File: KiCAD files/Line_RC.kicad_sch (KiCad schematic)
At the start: 26 parts, among them IC1 ESP32-WROVER-E-N4R8, IC2 CP2102N-A02-GQFN28R, IC3 BC847BDW1T1G

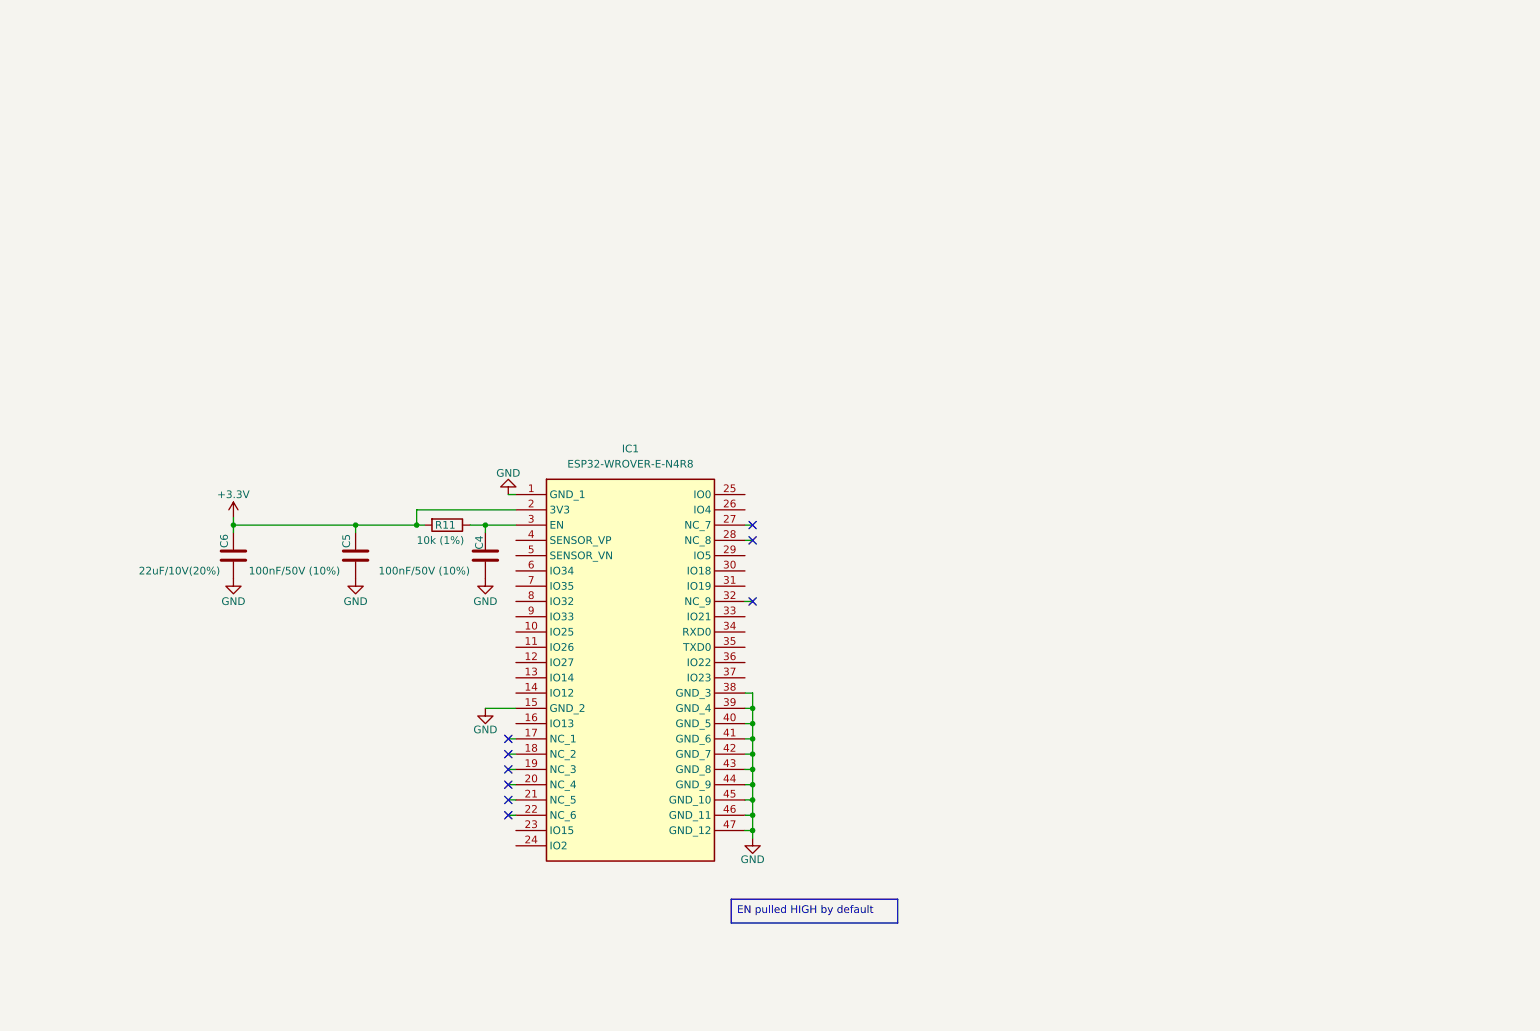
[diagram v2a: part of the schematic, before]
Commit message: Added power connectors
Added the power connectors for the LiPo battery and the ESC. Also added header pins for the selection of the internal / external Buck converter.
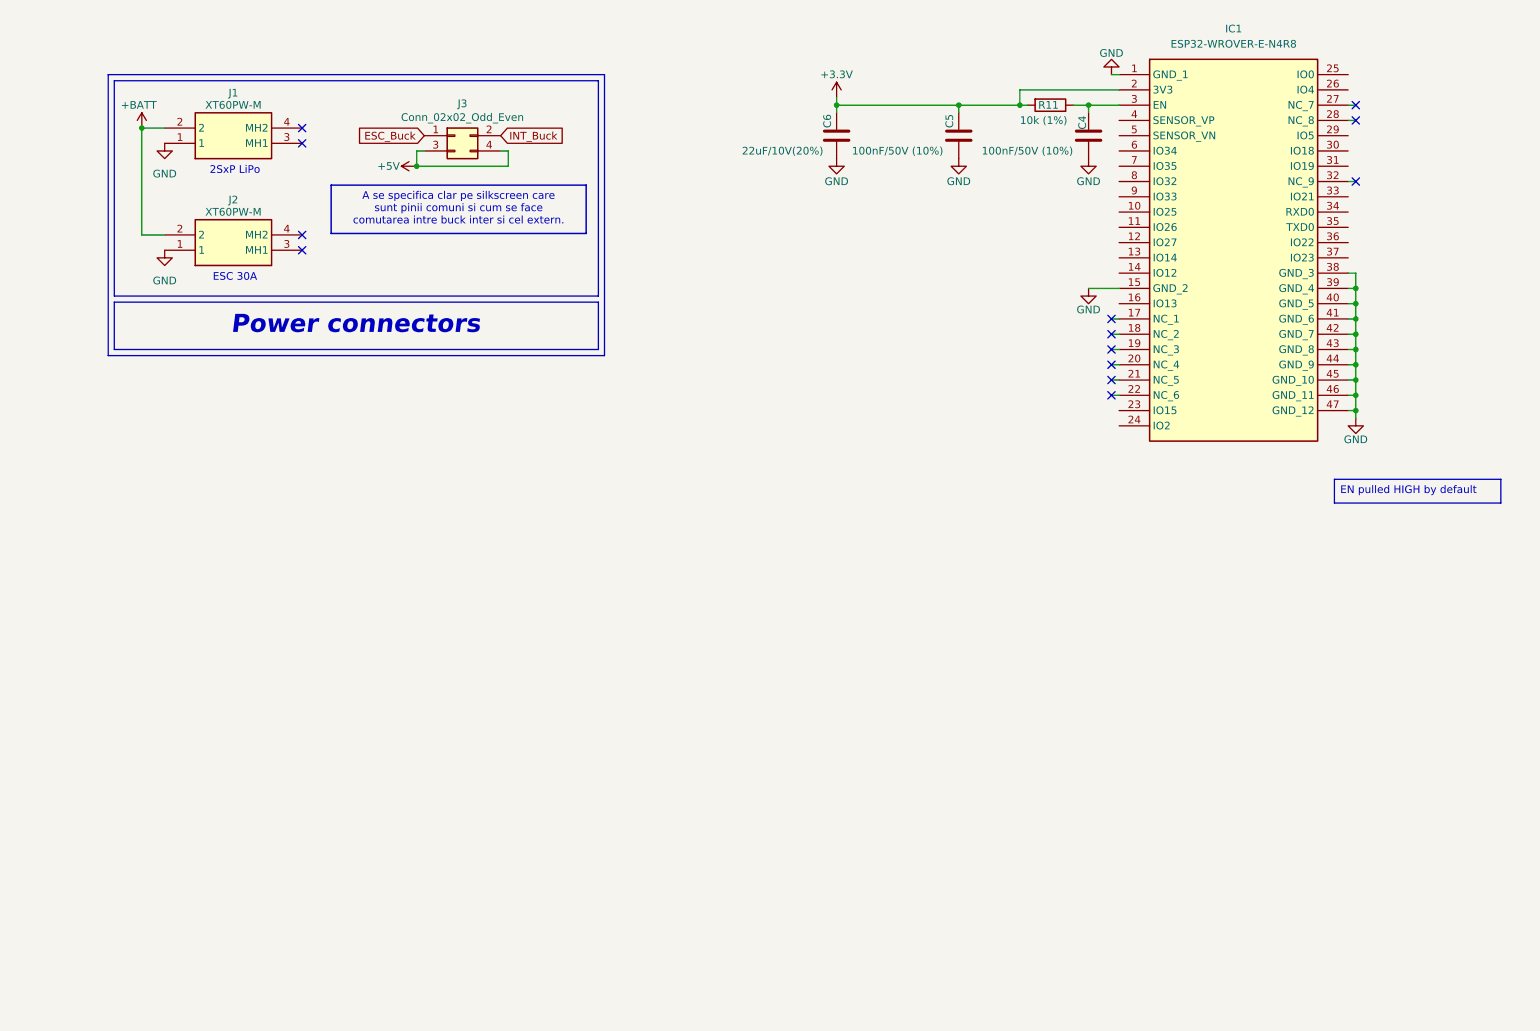
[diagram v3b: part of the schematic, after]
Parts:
- added J1, J2: XT60PW-M, XT60PWM, symbol XT60PW-M:XT60PW-M
- added J3: Conn_02x02_Odd_Even, Connector_PinHeader_1.27mm:PinHeader_2x02_P1.27mm_Vertical, symbol Connector_Generic:Conn_02x02_Odd_Even
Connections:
- net +5V: now also J3.3 (Pin_3), J3.4 (Pin_4)
- net GND: now also J1.1, J2.1
- new net +BATT: J1.2, J2.2
- new net ESC_Buck: J3.1 (Pin_1)
- new net INT_Buck: J3.2 (Pin_2)
- no-connect marks 29 -> 33
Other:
- note added: "2SxP LiPo"
- note added: "ESC 30A"
- note added: "Power connectors"
- moved on the sheet: C4, C5, C6, IC1, R11

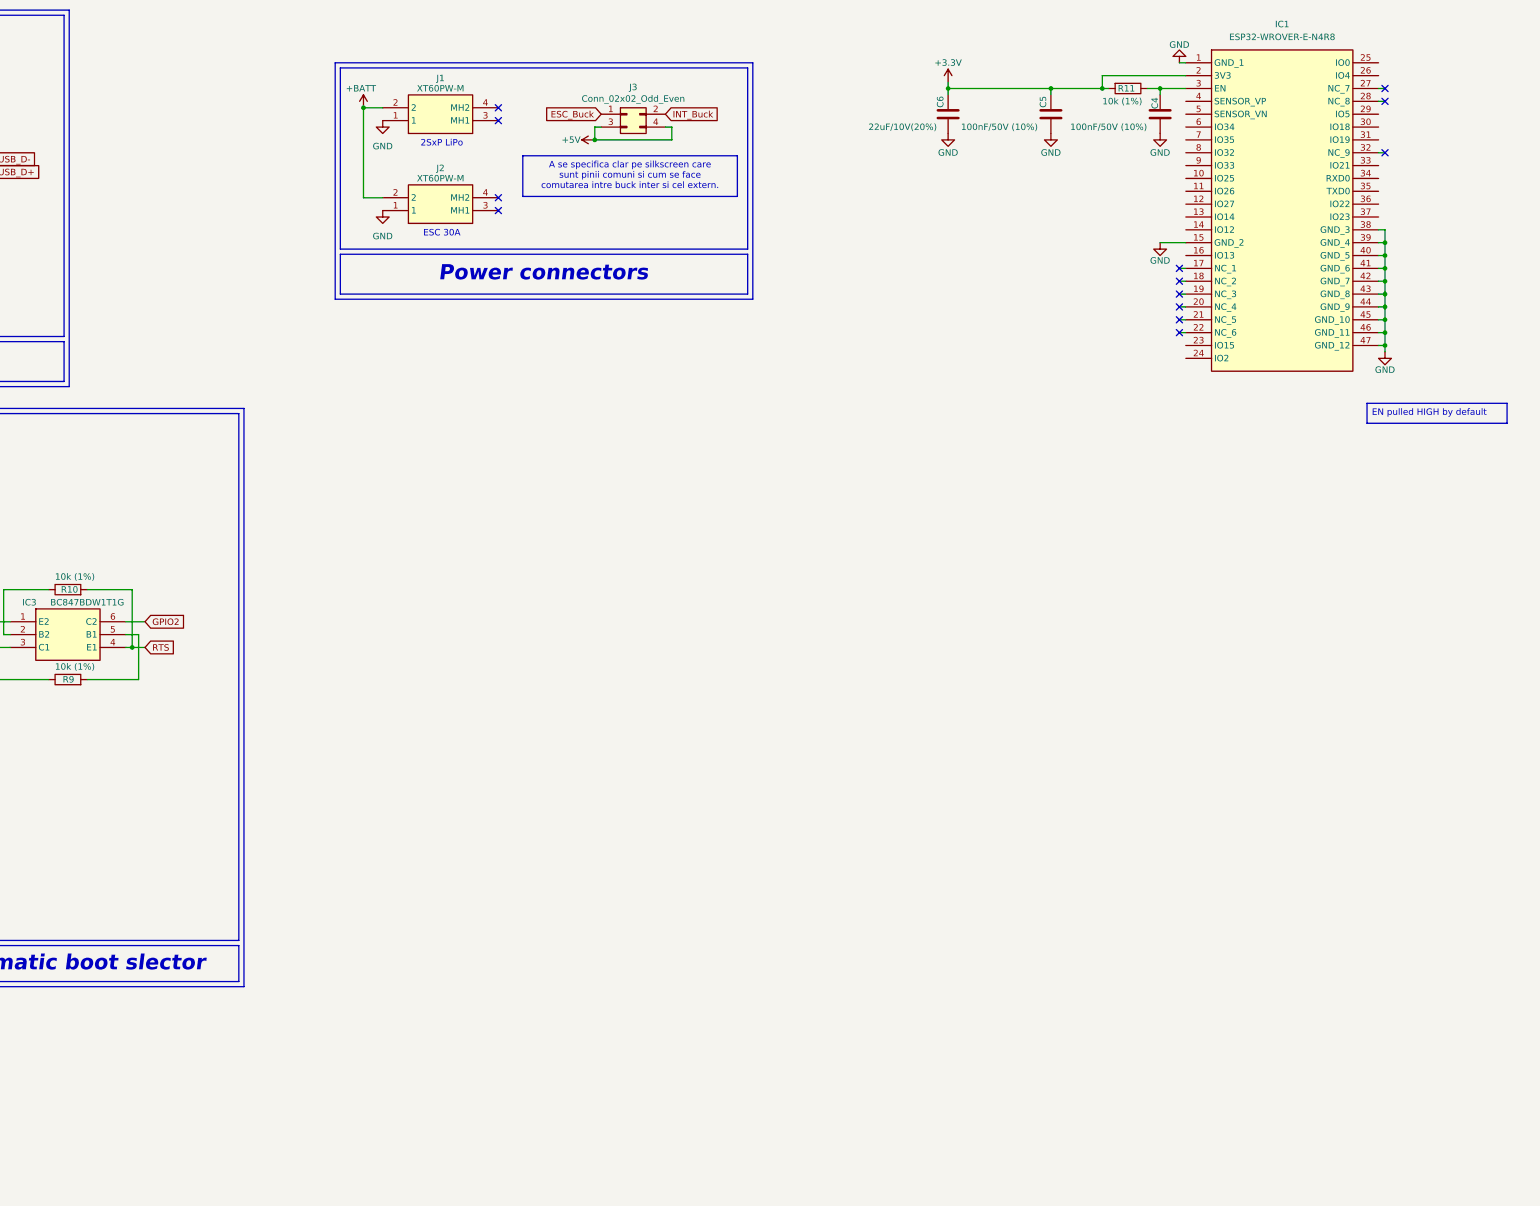
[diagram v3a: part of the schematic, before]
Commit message: added LDO and power connector
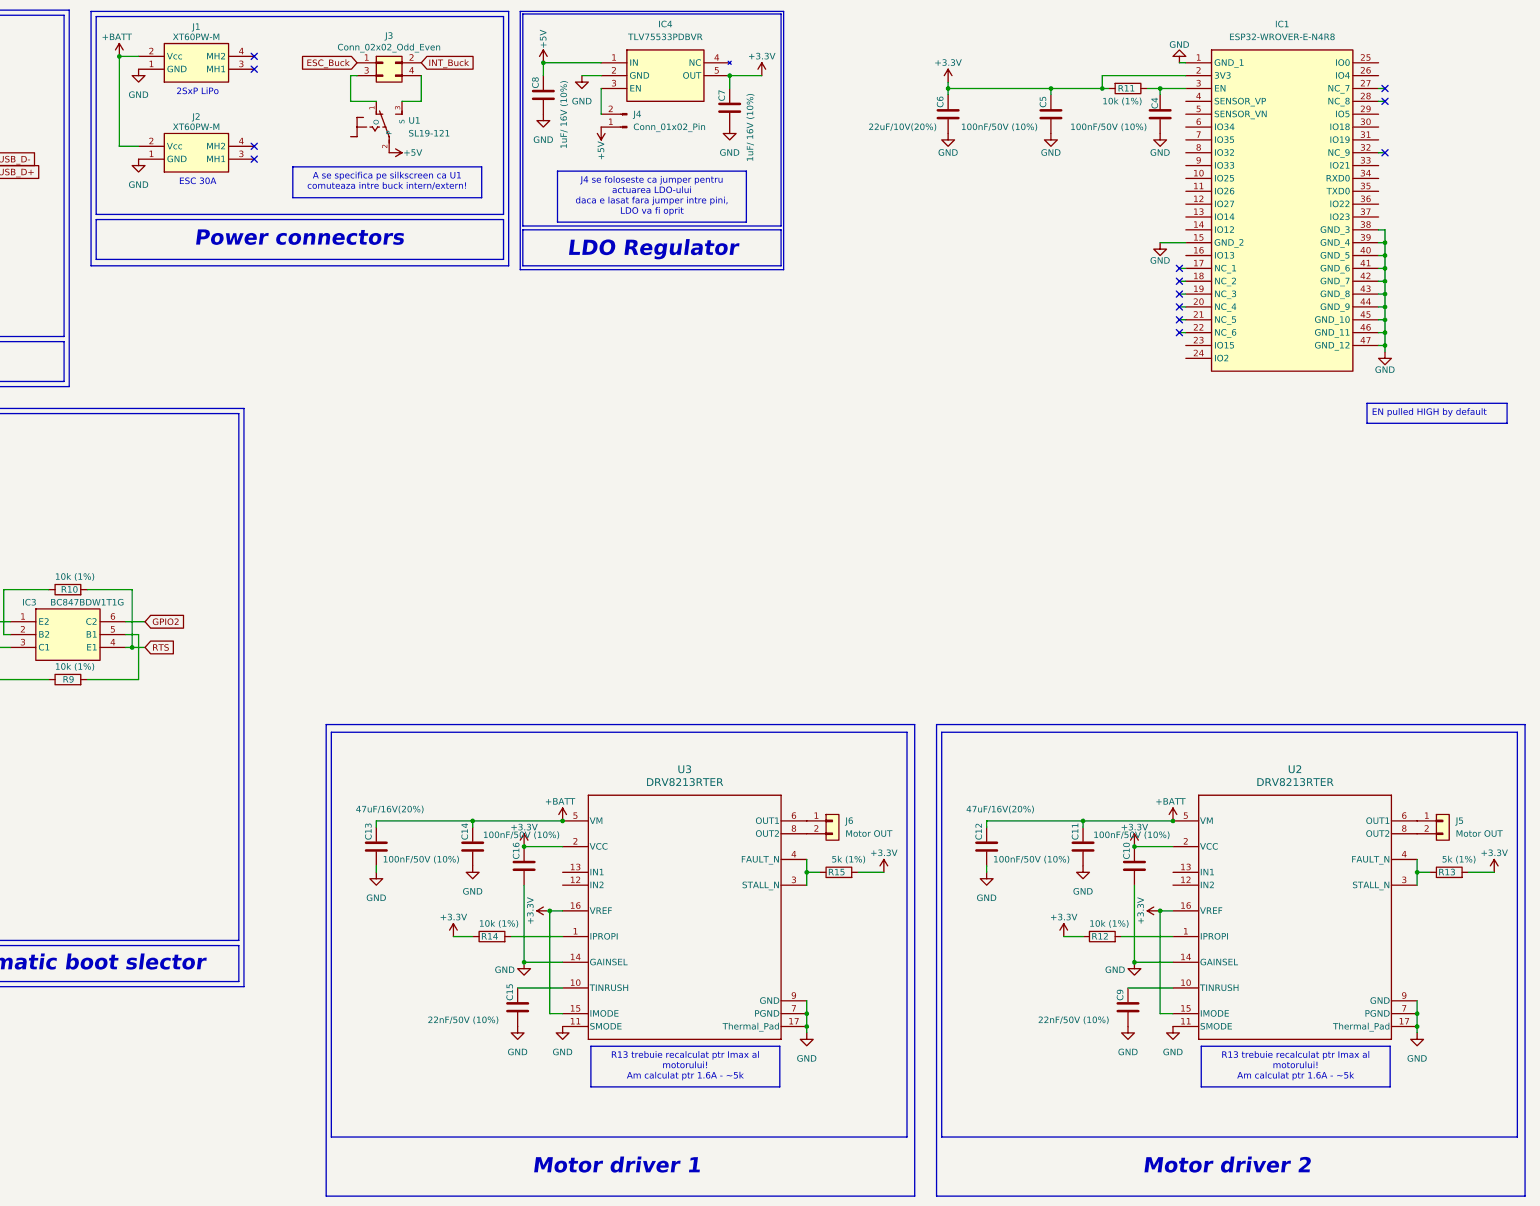
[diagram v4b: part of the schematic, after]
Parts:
- added C10, C11, C14, C16: 100nF/50V (10%), symbol Device:C
- added C12, C13: 47uF/16V(20%), symbol Device:C
- added C15, C9: 22nF/50V (10%), symbol Device:C
- added C7, C8: 1uF/ 16V (10%), symbol Device:C
- added IC4: TLV75533PDBVR, SOT95P280X145-5N, symbol TLV75533PDBVR:TLV75533PDBVR
- added J4: Conn_01x02_Pin, symbol Connector:Conn_01x02_Pin
- added J5, J6: Motor OUT, symbol Connector_Generic:Conn_01x02
- added R12, R14: 10k (1%), symbol Device:R
- added R13, R15: 5k (1%), symbol Device:R
- added U1: SL19-121, SL19-121:255SB, symbol SL19-121:SL19-121
- added U2, U3: DRV8213RTER, RTE0016C-IPC_A, symbol 2026-07-26_14-19-18:DRV8213RTER
- IC1: footprint ESP32WROVEREN4R8 -> ESP32-WROVER-E-N4R8:ESP32WROVEREN4R8
- IC2: footprint QFN50P500X500X80-29N-D -> CP2102N-A02-GQFN28:QFN50P500X500X80-29N-D
- IC3: footprint SOT65P210X110-6N -> BC847BDW1T1G:SOT65P210X110-6N
- J1, J2: footprint XT60PWM -> XT60PW-M:XT60PWM
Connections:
- net +3.3V: now also C10.1, C16.1, C7.1, IC4.5 (OUT), R12.1, R13.2, R14.1, R15.2, U2.15 (IMODE), U2.16 (VREF), U2.2 (VCC), U3.15 (IMODE), U3.16 (VREF), U3.2 (VCC)
- net +5V: now also C8.1, IC4.1 (IN), J4.1 (Pin_1), U1.2 (P); no longer J3.3 (Pin_3), J3.4 (Pin_4)
- net +BATT: now also C11.1, C12.1, C13.1, C14.1, U2.5 (VM), U3.5 (VM)
- net GND: now also C10.2, C11.2, C12.2, C13.2, C14.2, C15.2, C16.2, C7.2, C8.2, C9.2, IC4.2 (GND), U2.11 (SMODE), U2.14 (GAINSEL), U2.17 (Thermal_Pad), U2.7 (PGND), U2.9 (GND), U3.11 (SMODE), U3.14 (GAINSEL), U3.17 (Thermal_Pad), U3.7 (PGND), U3.9 (GND)
- new net: J3.3 (Pin_3), U1.1 (O)
- new net: J3.4 (Pin_4), U1.3 (S)
- new net: IC4.3 (EN), J4.2 (Pin_2)
- new net: R14.2, U3.1 (IPROPI)
- new net: C15.1, U3.10 (TINRUSH)
- new net: R15.1, U3.3 (STALL_N), U3.4 (FAULT_N)
- new net: J6.1 (Pin_1), U3.6 (OUT1)
- new net: J6.2 (Pin_2), U3.8 (OUT2)
- new net: C9.1, U2.10 (TINRUSH)
- new net: R13.1, U2.3 (STALL_N), U2.4 (FAULT_N)
- new net: J5.1 (Pin_1), U2.6 (OUT1)
- new net: J5.2 (Pin_2), U2.8 (OUT2)
- new net: R12.2, U2.1 (IPROPI)
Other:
- note added: "LDO Regulator"
- note added: "Motor driver 1"
- note added: "Motor driver 2"
- moved on the sheet: J1, J2, J3

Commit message: Added LDO and Buck, also improved readability
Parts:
- removed C12: 47uF/16V(20%), symbol Device:C
- removed J4: Conn_01x02_Pin, symbol Connector:Conn_01x02_Pin
- removed J5: Motor OUT, symbol Connector_Generic:Conn_01x02
- removed R3, R4: 0, symbol Device:R
- removed U2: DRV8213RTER, RTE0016C-IPC_A, symbol 2026-07-26_14-19-18:DRV8213RTER
- added C17: 47uF/16V, symbol Device:C
- added C18, C20: 100nF/50V, symbol Device:C
- added C19: 22nF/50V, symbol Device:C
- added IC5: ST1S40IPHR, SOIC127P600X175-9N, symbol ST1S40IPHR:ST1S40IPHR
- added J7: Motor OUT, symbol Connector_Generic:Conn_01x02
- added JP2: Solder Bridge, symbol Jumper:SolderJumper_2_Bridged
- added L1: 3.3uH, symbol Device:L
- added R16: 10k (1%), symbol Device:R
- added R17: 5k (1%), symbol Device:R
- added R18: 20K, symbol Device:R
- added U4: DRV8213RTER, RTE0016C-IPC_A, symbol 2026-07-26_14-19-18:DRV8213RTER
- C10: value 100nF/50V (10%) -> 10uF/25V
- C11: value 100nF/50V (10%) -> 22uF/25V
- C13: value 47uF/16V(20%) -> 47uF/16V
- C14, C16, C4, C5: value 100nF/50V (10%) -> 100nF/50V
- C15: value 22nF/50V (10%) -> 22nF/50V
- C2: value 10uF/25V (20%) -> 10uF/25V
- C6: value 22uF/10V(20%) -> 22uF/10V
- C7, C8: value 1uF/ 16V (10%) -> 1uF/ 16V
- C9: value 22nF/50V (10%) -> 1uF/25V
- R12: value 10k (1%) -> 10K
- R13: value 5k (1%) -> 62.5K
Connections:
- net +3.3V: now also C20.1, R16.1, R17.2, U4.15 (IMODE), U4.16 (VREF), U4.2 (VCC); no longer C10.1, R12.1, R13.2
- net +5V: now also C10.1, C9.1, R12.1, IC5.1 (VINA), IC5.6 (VINSW), JP2.1 (A)
- net +BATT: now also C17.1, C18.1, U4.5 (VM); no longer C11.1
- net GND: now also C17.2, C18.2, C19.2, C20.2, IC5.4 (GND), IC5.8 (PGND), IC5.9 (EPAD), R18.1, U4.11 (SMODE), U4.14 (GAINSEL), U4.17 (Thermal_Pad), U4.7 (PGND), U4.9 (GND)
- net USB_D+: now also D3.2 (A2), Q1. (MID)
- net USB_D-: now also D2.2 (A2), Q1. (MID)
- net at IC4.3 (EN): now also JP2.2 (B)
- net at R13.1: now also IC5.3 (FB), R18.2
- net at R12.2: now also IC5.2 (EN)
- removed net USB_DN: D2.2 (A2), Q1. (MID)
- removed net USB_DP: D3.2 (A2), Q1. (MID)
- new net: R16.2, U4.1 (IPROPI)
- new net: J7.1 (Pin_1), U4.6 (OUT1)
- new net: J7.2 (Pin_2), U4.8 (OUT2)
- new net: IC5.7 (SW), L1.1
- new net: C19.1, U4.10 (TINRUSH)
- new net: R17.1, U4.3 (STALL_N), U4.4 (FAULT_N)
- new net +3.3V-Int: C11.1, L1.2, R13.2
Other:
- note added: "Electronica de putere"
- note added: "Internal Buck Converter"
- note removed: "Motor driver 2"
- moved on the sheet: C1, C13, C14, C15, C16, C2, C3, C4, C5, C6, C7, C8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
